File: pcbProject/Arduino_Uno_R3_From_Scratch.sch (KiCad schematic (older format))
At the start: 0 parts

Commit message: af
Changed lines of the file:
@@
 F1 "ATMEGA328P.sch" 50
 F2 "AREF" I R 7050 2700 60
-F3 "SERIAL_Rx" I L 5550 3900 60
-F4 "SERIAL_Tx" I L 5550 4150 60
-F5 "ARD_AN5/SCL" I R 7050 5150 60
-F6 "ARD_AN4/SDA" I R 7050 5300 60
-F7 "ARD_AN3" I R 7050 5450 60
-F8 "ARD_AN2" I R 7050 5600 60
-F9 "ARD_AN1" I R 7050 5750 60
-F10 "ARD_AN0" I R 7050 5900 60
-F11 "ARD_DIG7" I R 7050 3850 60
-F12 "ARD_DIG6" I R 7050 4000 60
-F13 "ARD_DIG5" I R 7050 4150 60
-F14 "ARD_DIG4" I R 7050 4300 60
-F15 "ARD_DIG3" I R 7050 4450 60
-F16 "ARD_DIG2" I R 7050 4600 60
-F17 "ARD_DIG1" I R 7050 4750 60
-F18 "ARD_DIG0" I R 7050 4900 60
-F19 "ARD_DIG8" I R 7050 3600 60
-F20 "ARD_DIG9" I R 7050 3450 60
-F21 "ARD_DIG10/SPI_SS" I R 7050 3300 60
-F22 "ARD_DIG11/SPI_MOSI" I R 7050 3150 60
-F23 "ARD_DIG12/SPI_MISO" I R 7050 3000 60
-F24 "ARD_DIG13/SPI_SCK" I R 7050 2850 60
-F25 "DTR" I L 5550 3650 60
-F26 "328P_RESET" I R 7050 6150 60
+F3 "ARD_AN5/SCL" I R 7050 5150 60
+F4 "ARD_AN4/SDA" I R 7050 5300 60
+F5 "ARD_AN3" I R 7050 5450 60
+F6 "ARD_AN2" I R 7050 5600 60
+F7 "ARD_AN1" I R 7050 5750 60
+F8 "ARD_AN0" I R 7050 5900 60
+F9 "ARD_DIG7" I R 7050 3850 60
+F10 "ARD_DIG6" I R 7050 4000 60
+F11 "ARD_DIG5" I R 7050 4150 60
+F12 "ARD_DIG4" I R 7050 4300 60
+F13 "ARD_DIG3" I R 7050 4450 60
+F14 "ARD_DIG2" I R 7050 4600 60
+F15 "ARD_DIG1" I R 7050 4750 60
+F16 "ARD_DIG0" I R 7050 4900 60
+F17 "ARD_DIG8" I R 7050 3600 60
+F18 "ARD_DIG9" I R 7050 3450 60
+F19 "ARD_DIG10/SPI_SS" I R 7050 3300 60
+F20 "ARD_DIG11/SPI_MOSI" I R 7050 3150 60
+F21 "ARD_DIG12/SPI_MISO" I R 7050 3000 60
+F22 "ARD_DIG13/SPI_SCK" I R 7050 2850 60
+F23 "328P_RESET" I R 7050 6150 60
 $EndSheet
 Wire Wire Line

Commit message: schema Afgewerkt
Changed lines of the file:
@@
 F0 "Headers" 50
 F1 "Headers.sch" 50
-F2 "328P_RESET" I L 7550 6150 60
-F3 "ARD_AN5/SCL" I L 7550 5150 60
-F4 "ARD_AN4/SDA" I L 7550 5300 60
+F2 "328P_RESET" I L 7550 6275 60
+F3 "ARD_AN5/SCL" I L 7550 5550 60
+F4 "ARD_AN4/SDA" I L 7550 5650 60
 F5 "AREF" I L 7550 2700 60
 F6 "ARD_DIG13/SPI_SCK" I L 7550 2850 60
@@
 F10 "ARD_DIG9" I L 7550 3450 60
 F11 "ARD_DIG8" I L 7550 3600 60
-F12 "ARD_AN3" I L 7550 5450 60
-F13 "ARD_AN2" I L 7550 5600 60
-F14 "ARD_AN1" I L 7550 5750 60
-F15 "ARD_AN0" I L 7550 5900 60
+F12 "ARD_AN3" I L 7550 5750 60
+F13 "ARD_AN2" I L 7550 5850 60
+F14 "ARD_AN1" I L 7550 5975 60
+F15 "ARD_AN0" I L 7550 6100 60
 F16 "ARD_DIG7" I L 7550 3850 60
 F17 "ARD_DIG6" I L 7550 4000 60
@@
 F22 "ARD_DIG1" I L 7550 4750 60
 F23 "ARD_DIG0" I L 7550 4900 60
+F24 "ARD_AN6" I L 7550 5350 50
+F25 "ARD_AN7" I L 7550 5450 50
 $EndSheet
 $Sheet
@@
 F1 "ATMEGA328P.sch" 50
 F2 "AREF" I R 7050 2700 60
-F3 "ARD_AN5/SCL" I R 7050 5150 60
-F4 "ARD_AN4/SDA" I R 7050 5300 60
-F5 "ARD_AN3" I R 7050 5450 60
-F6 "ARD_AN2" I R 7050 5600 60
-F7 "ARD_AN1" I R 7050 5750 60
-F8 "ARD_AN0" I R 7050 5900 60
+F3 "ARD_AN5/SCL" I R 7050 5550 60
+F4 "ARD_AN4/SDA" I R 7050 5650 60
+F5 "ARD_AN3" I R 7050 5750 60
+F6 "ARD_AN2" I R 7050 5850 60
+F7 "ARD_AN1" I R 7050 5975 60
+F8 "ARD_AN0" I R 7050 6100 60
 F9 "ARD_DIG7" I R 7050 3850 60
 F10 "ARD_DIG6" I R 7050 4000 60
@@
 F21 "ARD_DIG12/SPI_MISO" I R 7050 3000 60
 F22 "ARD_DIG13/SPI_SCK" I R 7050 2850 60
-F23 "328P_RESET" I R 7050 6150 60
+F23 "328P_RESET" I R 7050 6275 60
+F24 "ARD_AN6" I R 7050 5450 50
+F25 "ARD_AN7" I R 7050 5350 50
 $EndSheet
 Wire Wire Line
@@
 Wire Wire Line
 	7050 4900 7550 4900
-Wire Wire Line
-	7550 5150 7050 5150
-Wire Wire Line
-	7050 5300 7550 5300
-Wire Wire Line
-	7550 5450 7050 5450
-Wire Wire Line
-	7050 5600 7550 5600
-Wire Wire Line
-	7550 5750 7050 5750
-Wire Wire Line
-	7050 5900 7550 5900
-Wire Wire Line
-	7550 6150 7050 6150
 $Sheet
 S 725  3350 1025 1900
@@
 Wire Wire Line
 	1950 7050 2150 7050
+Wire Wire Line
+	7050 6275 7550 6275
+Wire Wire Line
+	7050 6100 7550 6100
+Wire Wire Line
+	7050 5975 7550 5975
+Wire Wire Line
+	7050 5850 7550 5850
+Wire Wire Line
+	7050 5750 7550 5750
+Wire Wire Line
+	7050 5650 7550 5650
+Wire Wire Line
+	7050 5550 7550 5550
+Wire Wire Line
+	7050 5450 7550 5450
+Wire Wire Line
+	7050 5350 7550 5350
 $EndSCHEMATC

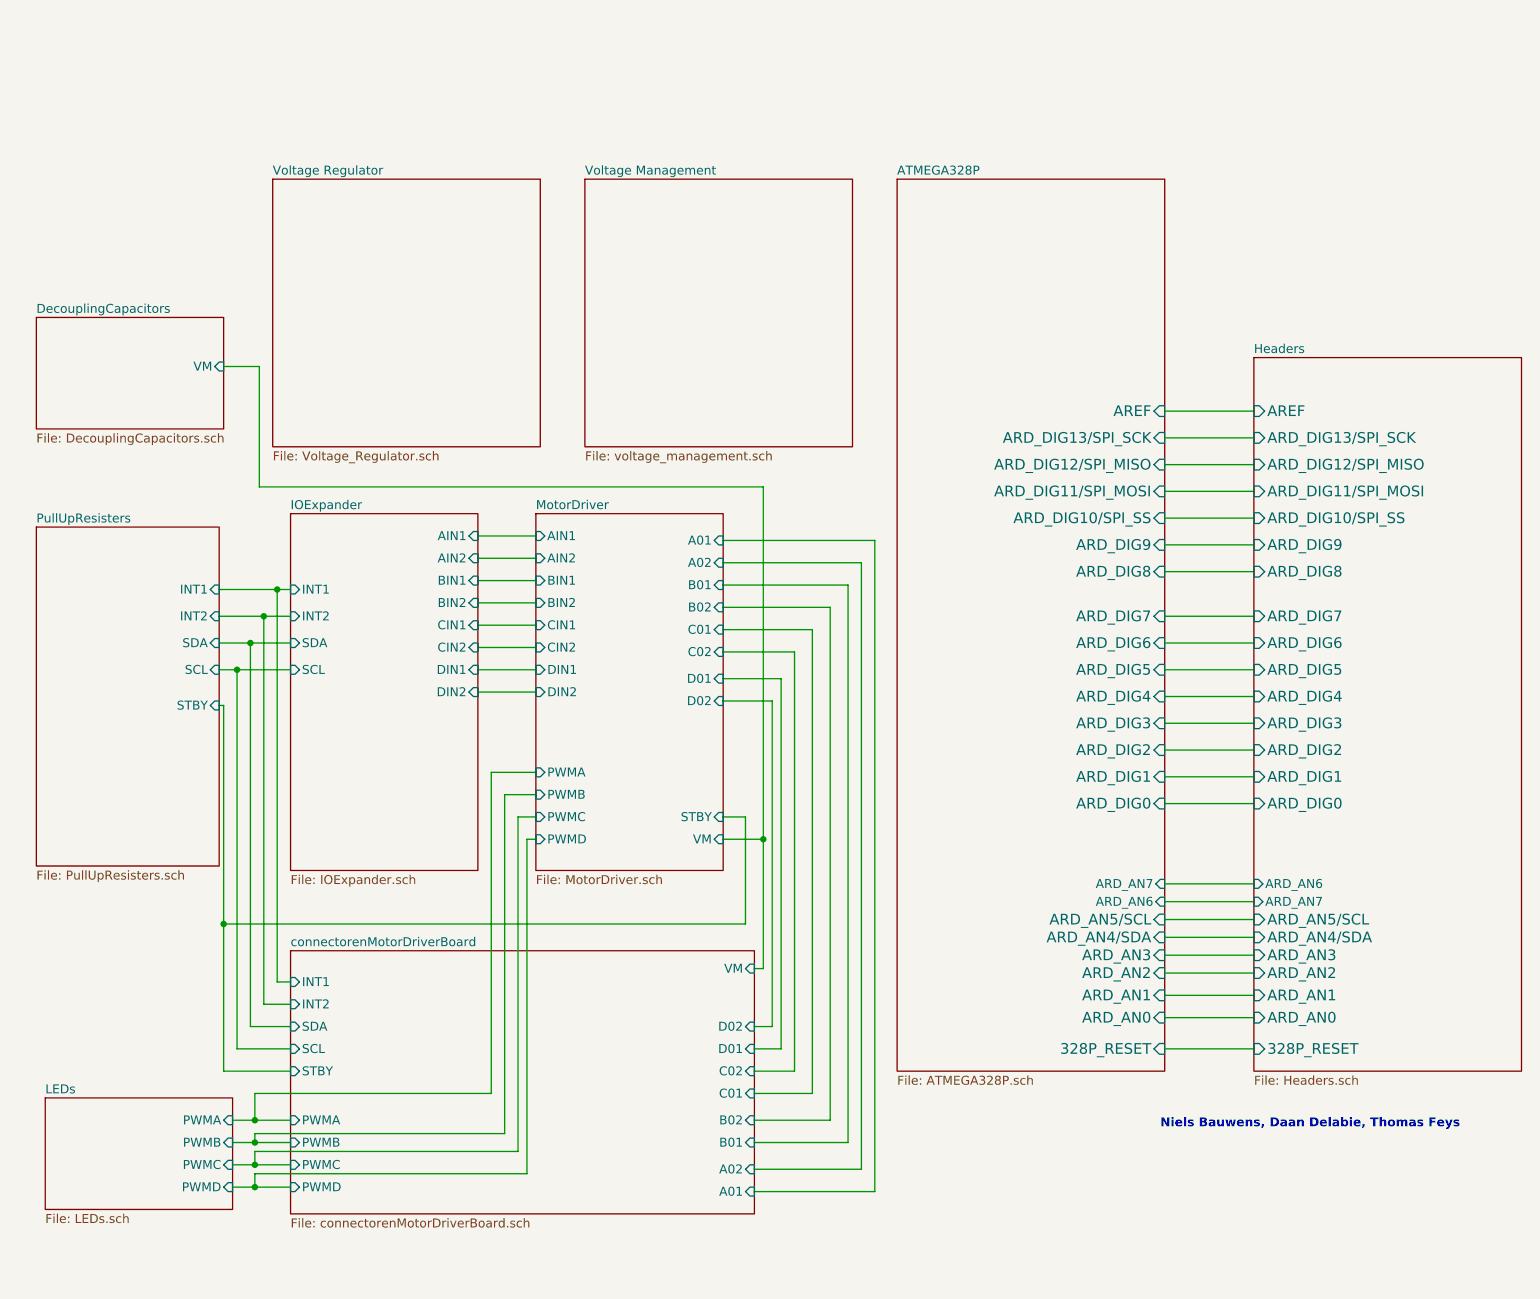
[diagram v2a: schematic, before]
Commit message: TekeningAfenGecontroleerd
nu nog componenten toevoegen en routen
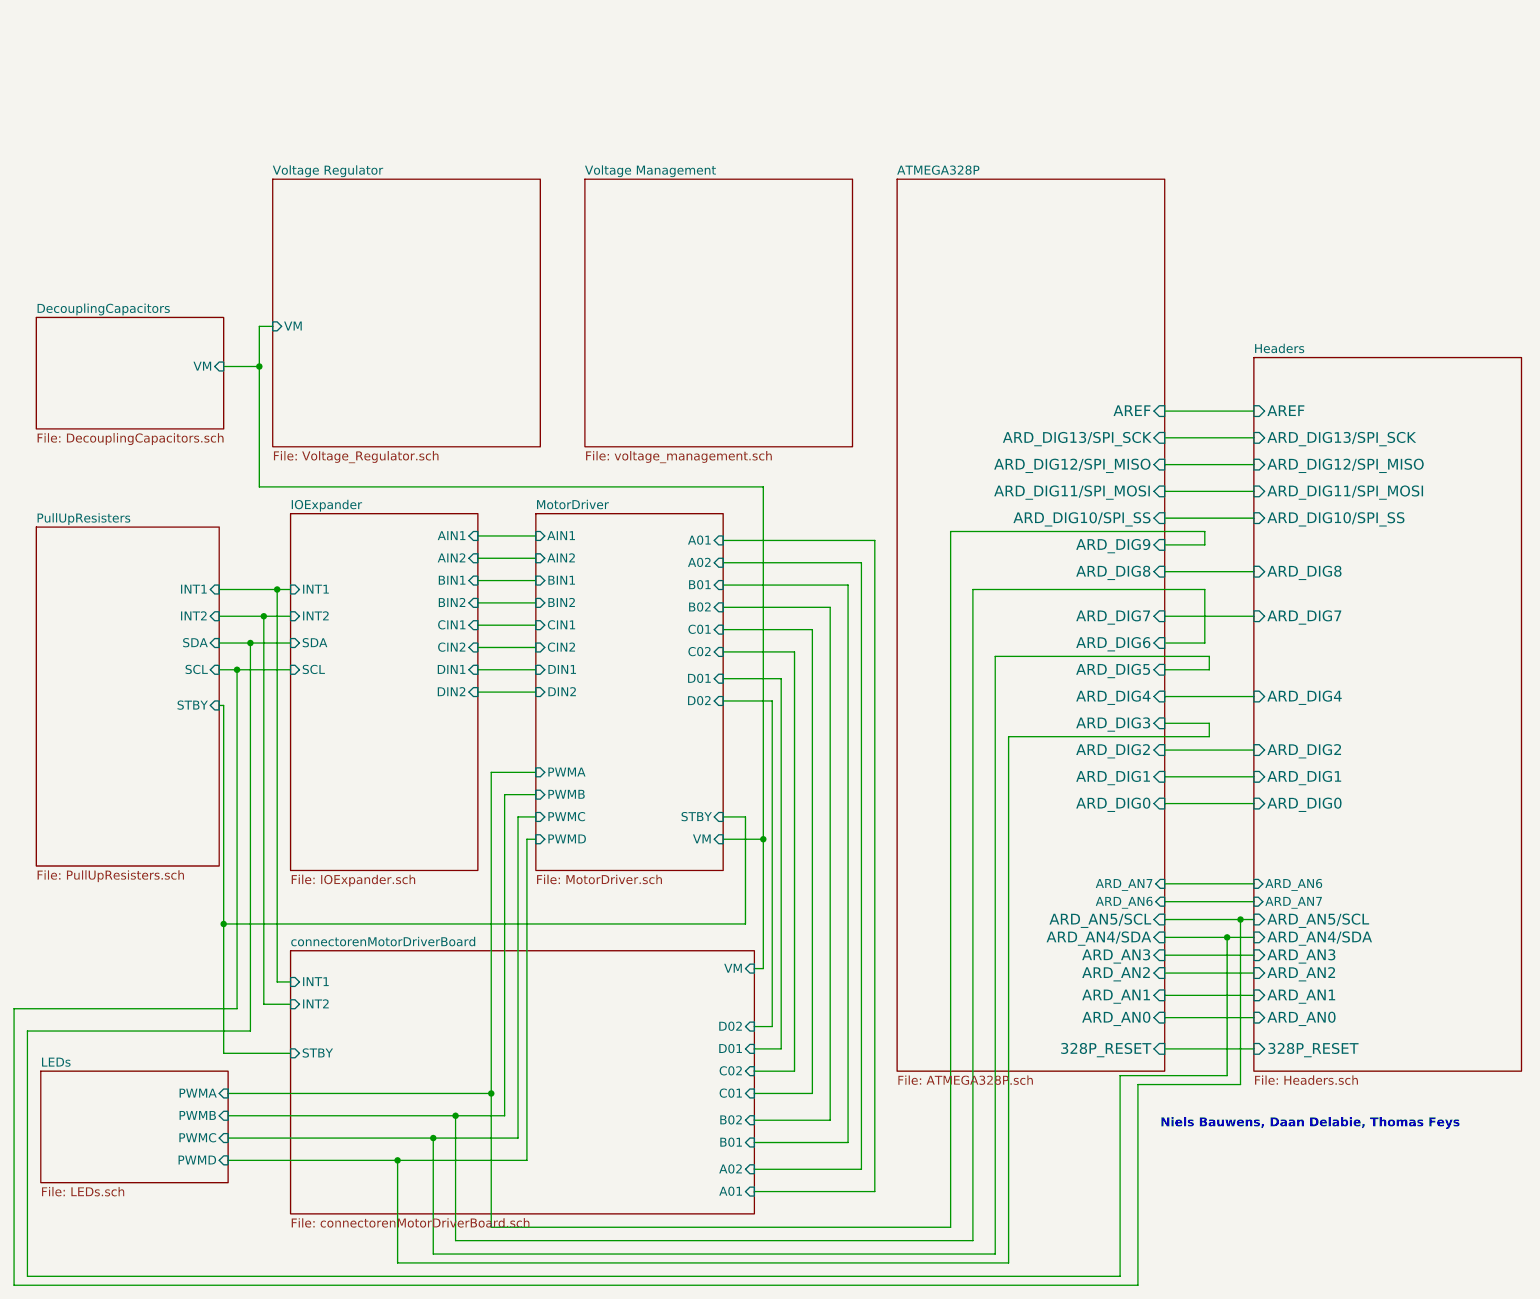
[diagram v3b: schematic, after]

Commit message: pcbAfgewerktVersie1
volledig afgewerkte pcb 1e versie
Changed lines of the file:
@@
 F18 "ARD_DIG1" I L 7550 4750 60
 F19 "ARD_DIG0" I L 7550 4900 60
-F20 "ARD_AN6" I L 7550 5350 50
-F21 "ARD_AN7" I L 7550 5450 50
+F20 "ARD_AN7" I L 7550 5350 50
+F21 "ARD_AN6" I L 7550 5450 50
 $EndSheet
 Wire Wire Line

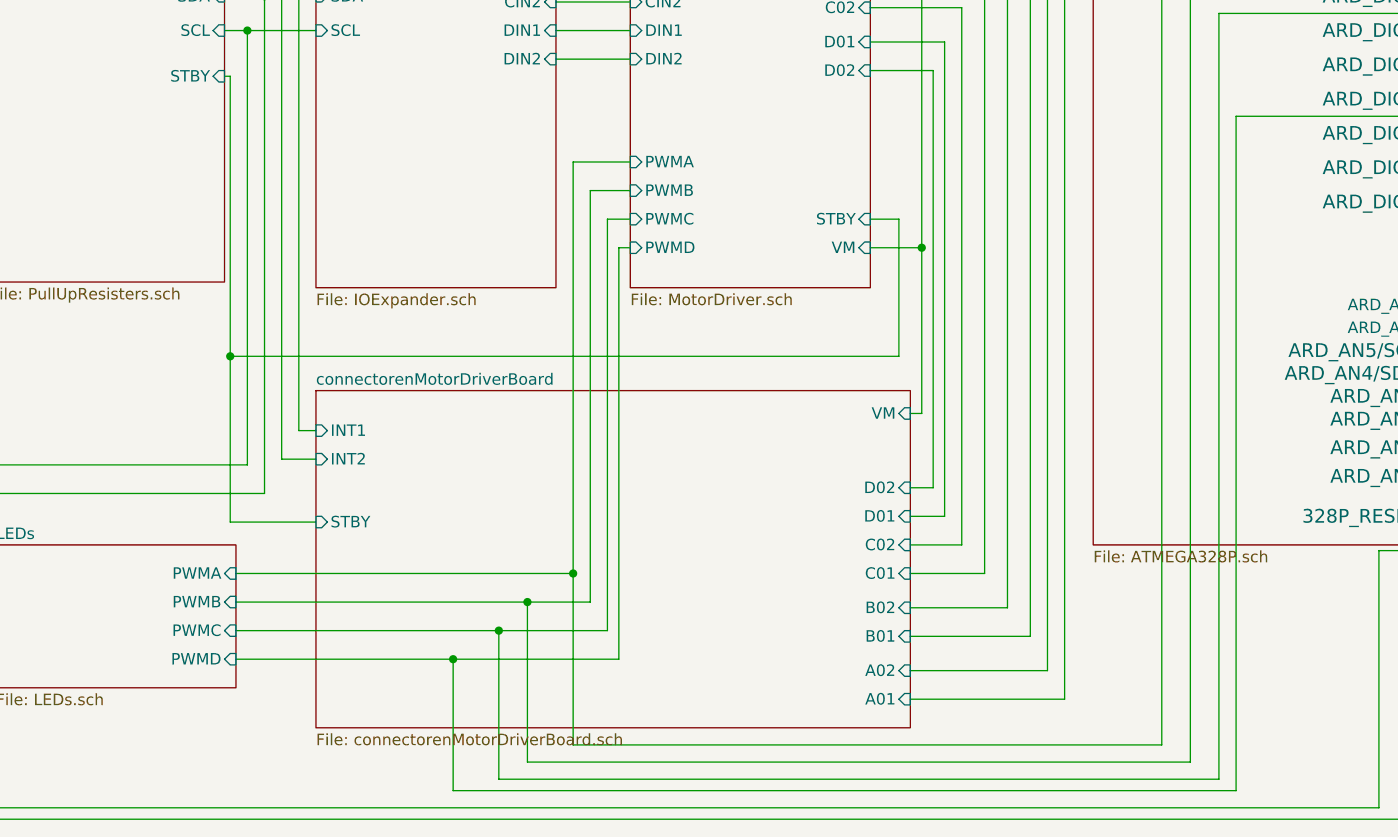
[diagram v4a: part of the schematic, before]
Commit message: PCB versie3
Aanpassingen tips coach --> veel gewijzigd
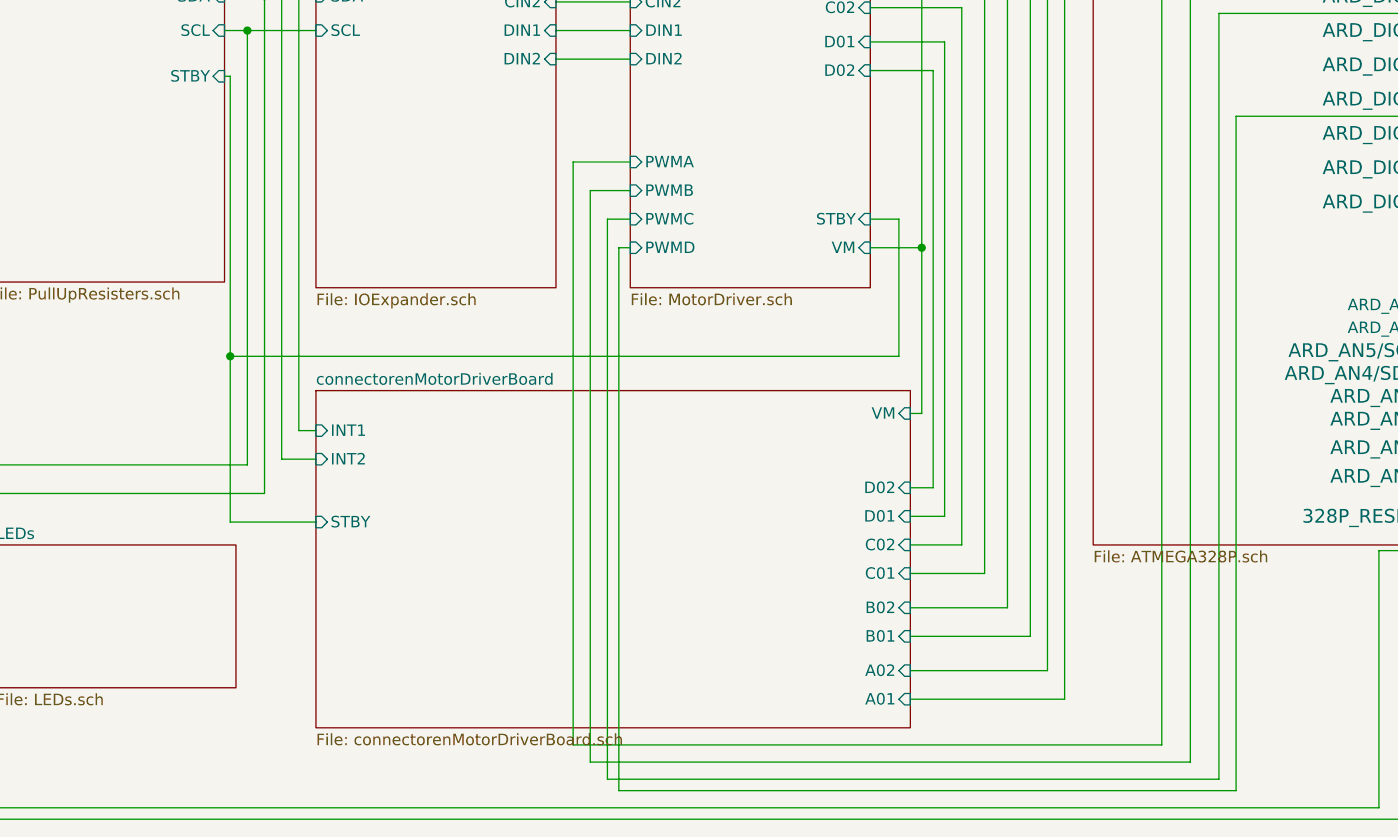
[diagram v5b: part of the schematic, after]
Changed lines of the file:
@@
 Connection ~ 4800 5100
-Wire Wire Line
-	3275 6525 3275 4725
 Wire Wire Line
 	3275 4725 3525 4725
@@
 	5850 7275 3275 7275
 Wire Wire Line
-	3275 7275 3275 6525
-Connection ~ 3275 6525
-Wire Wire Line
 	5975 3700 5975 7350
 Wire Wire Line
-	5975 7350 3075 7350
+	5975 7350 3350 7350
 Wire Wire Line
 	7300 4150 7300 4075
@@
 	6100 4075 6100 7425
 Wire Wire Line
-	6100 7425 2950 7425
+	6100 7425 3425 7425
 Wire Wire Line
 	7300 4150 7050 4150
@@
 	6175 4525 6175 7475
 Wire Wire Line
-	6175 7475 2750 7475
+	6175 7475 3475 7475
 Wire Wire Line
 	7300 4450 7050 4450
-Wire Wire Line
-	1800 6525 3275 6525
-Wire Wire Line
-	1800 6650 3075 6650
-Wire Wire Line
-	3350 6650 3350 4850
-Connection ~ 3075 6650
-Wire Wire Line
-	3075 6650 3350 6650
-$Sheet
-S 2150 5725 2600 1475
-U 5C6FDA9D
-F0 "connectorenMotorDriverBoard" 50
-F1 "connectorenMotorDriverBoard.sch" 50
-F2 "STBY" I L 2150 6300 50
-F3 "INT1" I L 2150 5900 50
-F4 "INT2" I L 2150 6025 50
-F5 "A01" I R 4750 7075 50
-F6 "A02" I R 4750 6950 50
-F7 "VM" I R 4750 5825 50
-F8 "D01" I R 4750 6275 50
-F9 "D02" I R 4750 6150 50
-F10 "B01" I R 4750 6800 50
-F11 "B02" I R 4750 6675 50
-F12 "C01" I R 4750 6525 50
-F13 "C02" I R 4750 6400 50
-$EndSheet
-Wire Wire Line
-	3075 6650 3075 7350
-Wire Wire Line
-	1800 6775 2950 6775
-Wire Wire Line
-	3425 6775 3425 4975
-Connection ~ 2950 6775
-Wire Wire Line
-	2950 6775 3425 6775
-Wire Wire Line
-	2950 6775 2950 7425
-Wire Wire Line
-	1800 6900 2750 6900
-Wire Wire Line
-	3475 6900 3475 5100
-Connection ~ 2750 6900
-Wire Wire Line
-	2750 6900 3475 6900
-Wire Wire Line
-	2750 6900 2750 7475
 Wire Wire Line
 	1750 4150 1850 4150
@@
 F0 "LEDs" 50
 F1 "LEDs.sch" 50
-F2 "PWMA" I R 1800 6525 50
-F3 "PWMB" I R 1800 6650 50
-F4 "PWMC" I R 1800 6775 50
-F5 "PWMD" I R 1800 6900 50
 $EndSheet
 Wire Wire Line
@@
 Wire Wire Line
 	7275 3700 5975 3700
+Wire Wire Line
+	3275 4725 3275 7275
+$Sheet
+S 2150 5725 2600 1475
+U 5C6FDA9D
+F0 "connectorenMotorDriverBoard" 50
+F1 "connectorenMotorDriverBoard.sch" 50
+F2 "STBY" I L 2150 6300 50
+F3 "INT1" I L 2150 5900 50
+F4 "INT2" I L 2150 6025 50
+F5 "A01" I R 4750 7075 50
+F6 "A02" I R 4750 6950 50
+F7 "VM" I R 4750 5825 50
+F8 "D01" I R 4750 6275 50
+F9 "D02" I R 4750 6150 50
+F10 "B01" I R 4750 6800 50
+F11 "B02" I R 4750 6675 50
+F12 "C01" I R 4750 6525 50
+F13 "C02" I R 4750 6400 50
+$EndSheet
+Wire Wire Line
+	3425 4975 3425 7425
+Wire Wire Line
+	3350 4850 3350 7350
+Wire Wire Line
+	3475 5100 3475 7475
 $EndSCHEMATC

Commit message: verslag
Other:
- note removed: "Niels Bauwens, Daan Delabie, Thomas Feys"
